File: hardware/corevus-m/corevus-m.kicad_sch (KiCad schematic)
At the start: 84 parts, among them J1 Power In, J1 USB 2.0, SW1 SPDT, SW3 SPST, T1 3.3V, T1 CS, T1 Diag, T1 Dir, T1 En, T1 Gnd, T1 MISO, T1 MOSI, T1 SClk, T1 Step, T1 V_{SA}, U1 STM32G431CBUx, U2 TPS61040DBV, U4 SRV05-4, U6 AMS1117-3.3, Y1 12 MHz

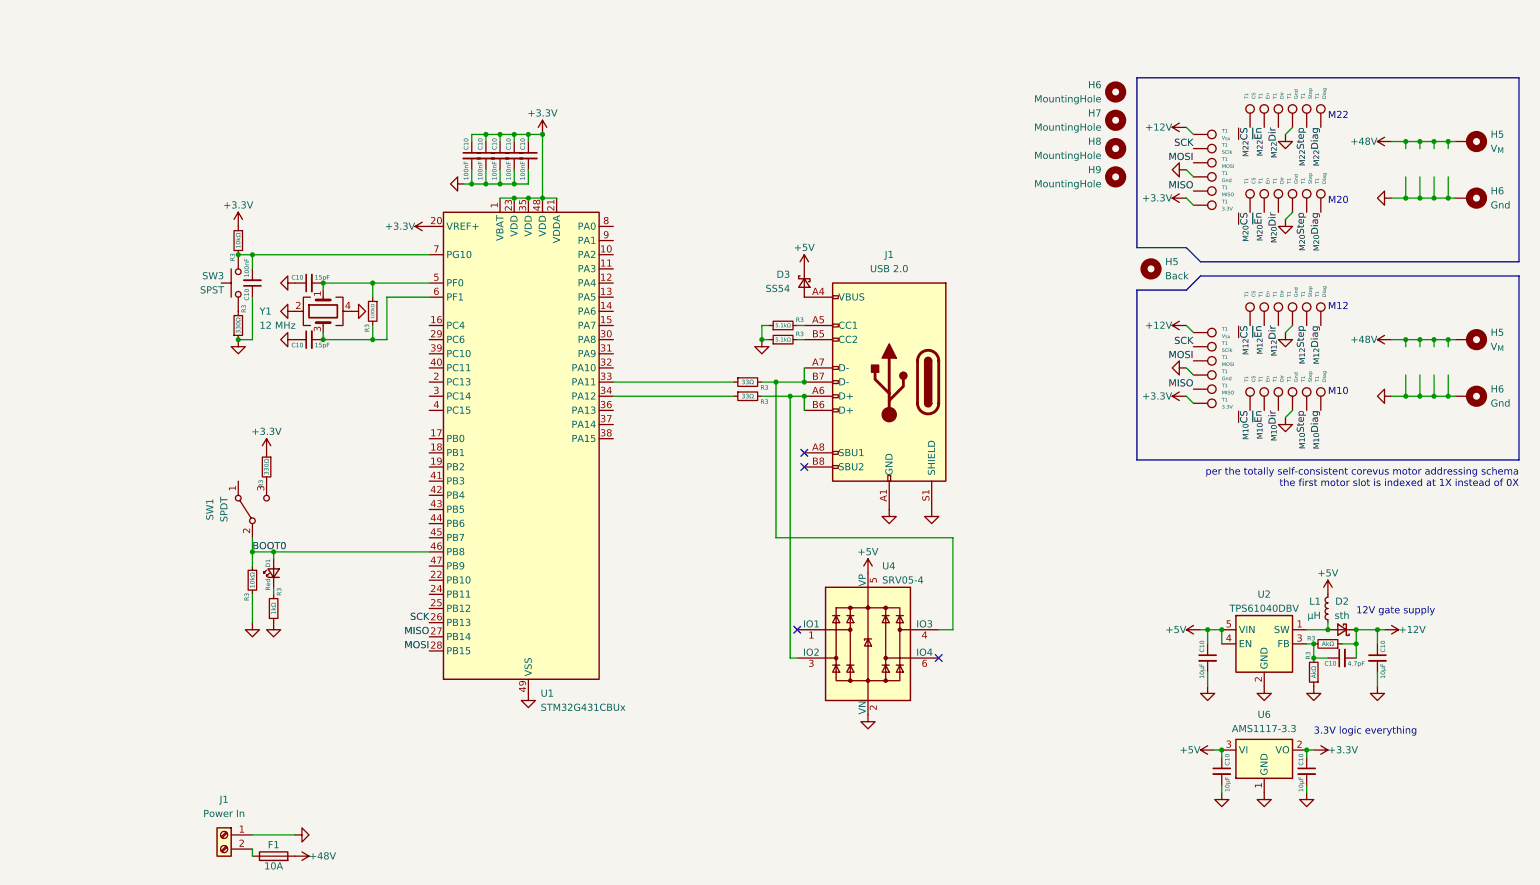
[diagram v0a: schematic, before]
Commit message: finish corevus-g, create file for corevus-k
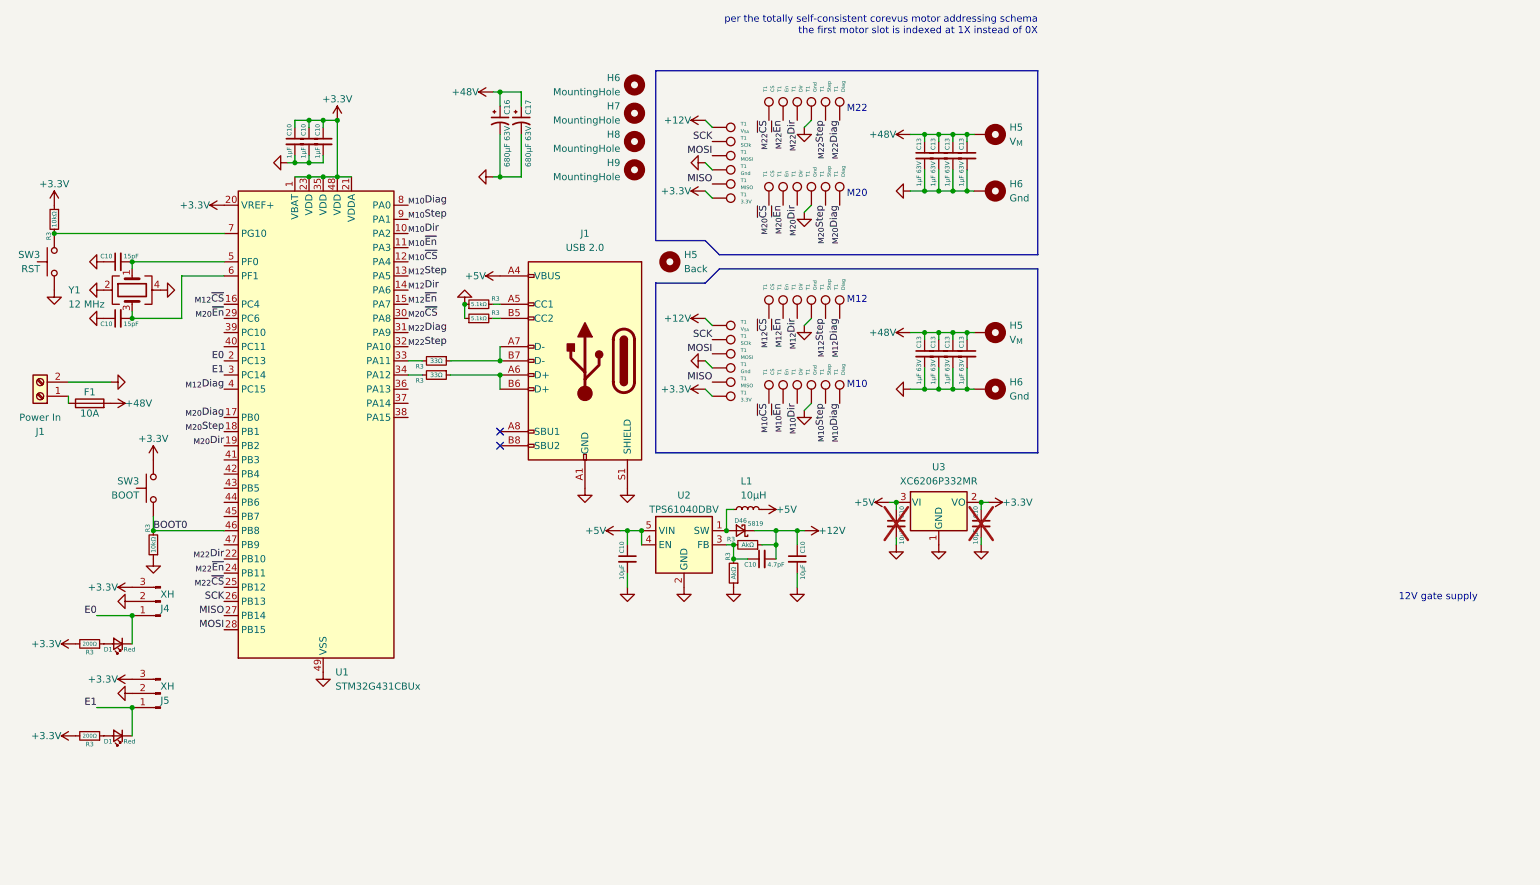
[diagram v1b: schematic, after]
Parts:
- removed C10 (x5): 100nF, AlphaLib:0402C, symbol Device:C_Small
- removed D1: Red, AlphaLib:0402LED, symbol Device:LED_Small
- removed D2: sth, symbol Device:D_Schottky_Small
- removed D3: SS54, Diode_SMD:D_SMA, symbol Device:D_Schottky_Small
- removed R3: 1kΩ, AlphaLib:0402R, symbol Device:R_Small
- removed R3 (x2): 330Ω, AlphaLib:0402R, symbol Device:R_Small
- removed R3: 100kΩ, AlphaLib:0402R, symbol Device:R_Small
- removed SW1: SPDT, corevus:MSS12C02-LS, symbol Switch:SW_SPDT
- removed U4: SRV05-4, Package_TO_SOT_SMD:SOT-23-6, symbol Power_Protection:SRV05-4
- removed U6: AMS1117-3.3, Package_TO_SOT_SMD:SOT-223-3_TabPin2, symbol Regulator_Linear:AMS1117-3.3
- added C10 (x2): 1µF, AlphaLib:0402C, symbol Device:C_Small
- added C13 (x8): 1μF 63V, Capacitor_SMD:C_1206_3216Metric, symbol Device:C_Small
- added C16, C17: 680μF 63V, corevus:CP_Radial_D12.5mm_P5.00mm_H20mm_Horizontal, symbol Device:C_Polarized_Small_US
- added D1 (x2): Red, AlphaLib:0603LED, symbol Device:LED_Small
- added D46: 5819, corevus:D_SOD-323, symbol Device:D_Schottky_Small
- added J4, J5: XH, corevus:JST_XH_1x03, symbol Connector:Conn_01x03_Pin
- added R3 (x2): 200Ω, AlphaLib:0402R, symbol Device:R_Small
- added SW3: BOOT, corevus:ShouHan_TS3315A, symbol Switch:SW_Push
- added U3: XC6206P332MR, Package_TO_SOT_SMD:SOT-23-3, symbol Regulator_Linear:XC6206PxxxMR
- C10: value 100nF -> 1µF
- C10: now not fitted; now left out of the parts list
- J1: footprint (none) -> corevus:Kefa_KF8500-8.5-2P
- L1: value µH -> 10µH; footprint (none) -> Inductor_SMD:L_0805_2012Metric
- SW3: value SPST -> RST; footprint corevus:XKB_TS-1187A -> corevus:ShouHan_TS3315A
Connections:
- net +12V: now also D46.1 (K)
- net +3.3V: now also C10.1, C10.1, J4.3 (Pin_3), J5.3 (Pin_3), R3.2, R3.2, SW3.2, U3.2 (VO)
- net +48V: now also C13.1, C13.1, C13.1, C13.1, C13.1, C13.1, C13.1, C13.1, C16.1, C17.1
- net +5V: now also J1.A4 (VBUS), J1.A9 (VBUS), J1.B4 (VBUS), J1.B9 (VBUS), U3.3 (VI)
- net BOOT0: now also R3.2, SW3.1; no longer R3.1
- net GND: now also J1.2 (Pin_2), R3.1, SW3.1, C10.2, C10.2, C13.2, C13.2, C13.2, C13.2, C13.2, C13.2, C13.2, C13.2, C16.2, C17.2, J4.2 (Pin_2), J5.2 (Pin_2), U3.1 (GND); no longer J1.1 (Pin_1), R3.2
- net _{M10}Diag: now also U1.8 (PA0)
- net _{M10}Dir: now also U1.10 (PA2)
- net _{M10}Step: now also U1.9 (PA1)
- net _{M10}~{CS}: now also U1.12 (PA4)
- net _{M10}~{En}: now also U1.11 (PA3)
- net _{M12}Diag: now also U1.4 (PC15)
- net _{M12}Dir: now also U1.14 (PA6)
- net _{M12}Step: now also U1.13 (PA5)
- net _{M12}~{CS}: now also U1.16 (PC4)
- net _{M12}~{En}: now also U1.15 (PA7)
- net _{M20}Diag: now also U1.17 (PB0)
- net _{M20}Dir: now also U1.19 (PB2)
- net _{M20}Step: now also U1.18 (PB1)
- net _{M20}~{CS}: now also U1.30 (PA8)
- net _{M20}~{En}: now also U1.29 (PC6)
- net _{M22}Diag: now also U1.31 (PA9)
- net _{M22}Dir: now also U1.22 (PB10)
- net _{M22}Step: now also U1.32 (PA10)
- net _{M22}~{CS}: now also U1.25 (PB12)
- net _{M22}~{En}: now also U1.24 (PB11)
- net at L1.2, U2.1 (SW): now also D46.2 (A)
- net at F1.1: now also J1.1 (Pin_1); no longer J1.2 (Pin_2)
- net at R3.1: now also J1.A7 (D-), J1.B7 (D-); no longer U1.33 (PA11)
- net at R3.1: now also J1.A6 (D+), J1.B6 (D+); no longer U1.34 (PA12)
- net E0: now reaches U1.2 (PC13)
- net E0: now also D1.1 (K), J4.1 (Pin_1)
- net E1: now reaches U1.3 (PC14)
- net E1: now also D1.1 (K), J5.1 (Pin_1)
- new net: D1.2 (A), R3.1 (x2)
- new net: R3.2, U1.33 (PA11)
- new net: R3.2, U1.34 (PA12)
- no-connect marks 4 -> 2
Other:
- note removed: "3.3V logic everything"
- moved on the sheet: C10, F1, H5, H6, H7, H8, H9, J1, L1, R3, SW3, T1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

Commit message: test
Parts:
- R3: value AkΩ -> 10kΩ
- R3: value AkΩ -> 100kΩ
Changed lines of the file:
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@@
       (effects (font (size 0.8 0.8)) (justify right))
     )
-    (property "Value" "AkΩ" (at 140.97 104.14 90)
-      (effects (font (size 0.8 0.8)))
+    (property "Value" "10kΩ" (at 140.97 104.14 90)
+      (effects (font (size 0.7 0.7)))
     )
     (property "Footprint" "AlphaLib:0402R" (at 140.97 104.14 0)
@@
       (effects (font (size 0.8 0.8)) (justify right))
     )
-    (property "Value" "AkΩ" (at 143.51 99.06 90)
-      (effects (font (size 0.8 0.8)))
+    (property "Value" "100kΩ" (at 143.51 99.06 90)
+      (effects (font (size 0.6 0.6)))
     )
     (property "Footprint" "AlphaLib:0402R" (at 143.51 99.06 0)
